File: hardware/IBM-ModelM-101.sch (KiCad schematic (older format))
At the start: 22 parts

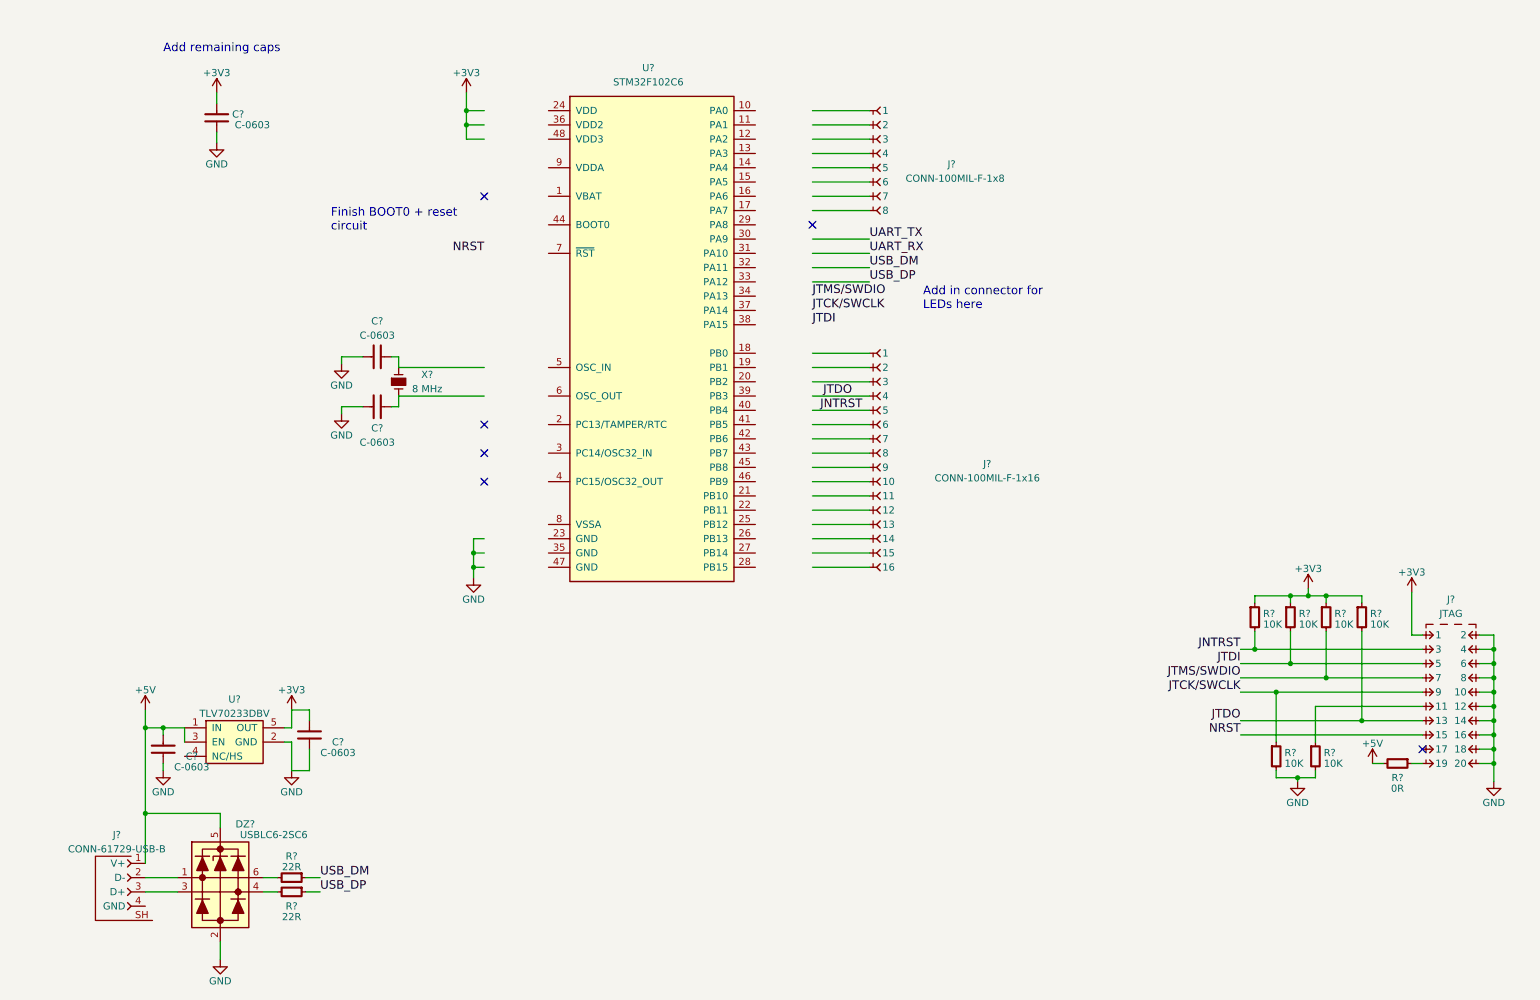
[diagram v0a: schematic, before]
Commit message: Finished power and boot/reset circuits
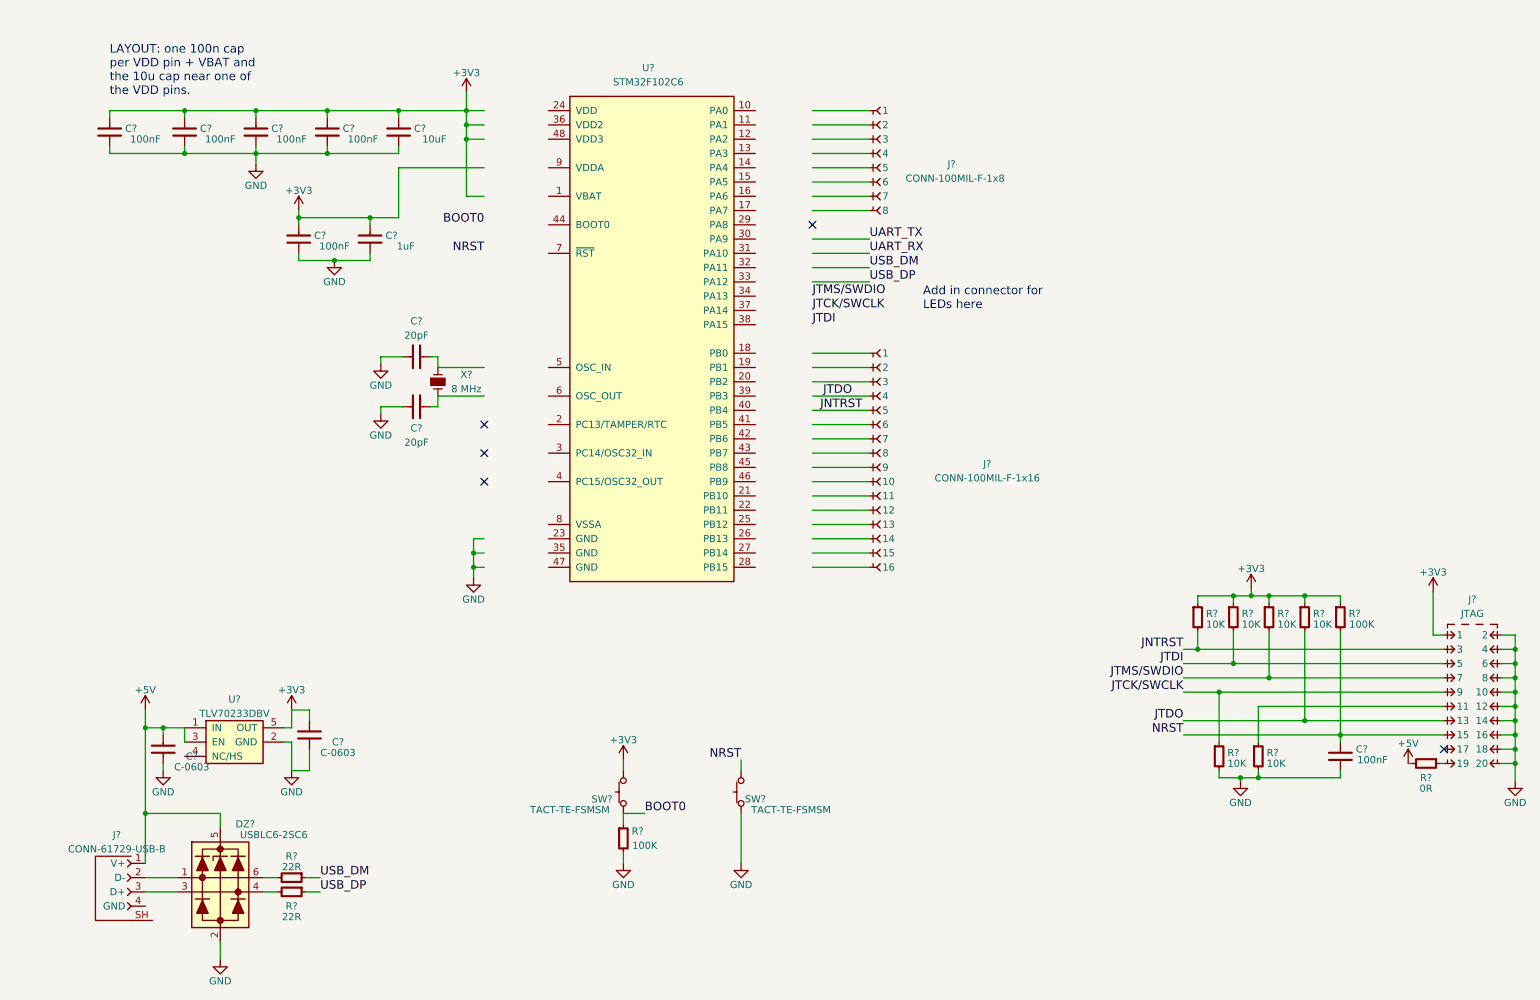
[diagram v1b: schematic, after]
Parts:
- added C? (x5): 100nF, IPC7351-Nominal:CAPC1608X55, symbol C-0603
- added C?: 10uF, IPC7351-Nominal:CAPC1608X55, symbol C-0603
- added C?: 1uF, IPC7351-Nominal:CAPC1608X55, symbol C-0603
- added R? (x2): 100K, IPC7351-Nominal:RESC1608X50, symbol R-0603
- added SW? (x2): TACT-TE-FSMSM, manuf:TE-FSMSM, symbol TACT-TE-FSMSM
- C? (x2): value C-0603 -> 20pF
- C?: value C-0603 -> 100nF
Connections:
- net labels added: BOOT0
- wire segments 108 -> 177
- no-connect marks 6 -> 5
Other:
- note added: "LAYOUT: one 100n cap\nper VDD pin + VBAT and\nthe 10u cap near one of \nthe VDD pins."
- note removed: "Add remaining caps"
- note removed: "Finish BOOT0 + reset\ncircuit"
- moved on the sheet: C?, J?, R?, X?

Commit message: Finished schematic, started work on PCB layout
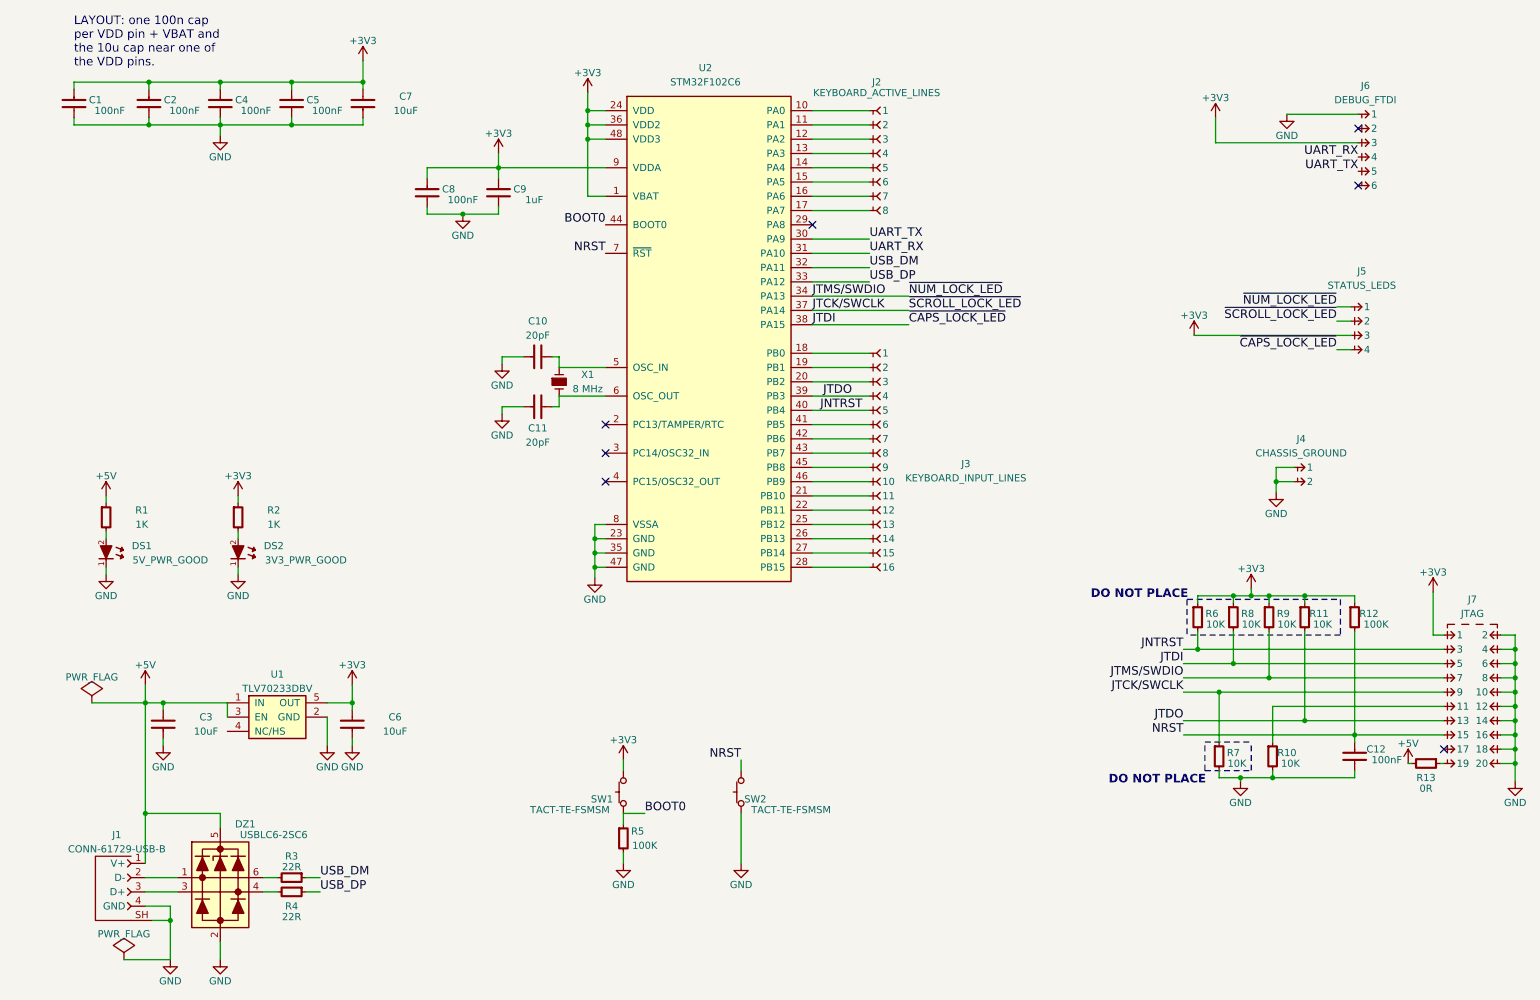
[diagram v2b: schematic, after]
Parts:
- removed C? (x2): C-0603, IPC7351-Nominal:CAPC1608X55, symbol C-0603
- removed C?: 10uF, IPC7351-Nominal:CAPC1608X55, symbol C-0603
- added C3, C6, C7: 10uF, IPC7351-Nominal:CAPC2012X70, symbol C-0805
- added DS1: 5V_PWR_GOOD, smd-semi:LED-0603, symbol LED-0603
- added DS2: 3V3_PWR_GOOD, smd-semi:LED-0603, symbol LED-0603
- added J4: CHASSIS_GROUND, conn-100mil:CONN-100MIL-M-1x2, symbol CONN-100MIL-M-1x2
- added J5: STATUS_LEDS, conn-100mil:CONN-100MIL-M-1x4-SHROUD, symbol CONN-100MIL-M-1x4-SHROUD
- added J6: DEBUG_FTDI, conn-100mil:CONN-100MIL-M-1x6, symbol CONN-100MIL-M-1x6
- added R1, R2: 1K, IPC7351-Nominal:RESC1608X50, symbol R-0603
- C1, C12, C2, C4, C5, C8: renamed from C?; BOM CAP MLCC 100pF C0G 50V 5% [0603] -> CAP MLCC 100nF C0G 6.3V 5% [0603]
- C9: renamed from C?; BOM CAP MLCC 100pF C0G 50V 5% [0603] -> CL10B105KQ8NNNC
- J2: renamed from J?; value CONN-100MIL-F-1x8 -> KEYBOARD_ACTIVE_LINES
- J3: renamed from J?; value CONN-100MIL-F-1x16 -> KEYBOARD_INPUT_LINES
- X1: renamed from X?; BOM (none) -> ATS08ASM-1E
- gave numbers to parts that had none: 20
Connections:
- net labels added: ~CAPS_LOCK_LED~, ~NUM_LOCK_LED~, ~SCROLL_LOCK_LED~
- wire segments 177 -> 155
- no-connect marks 5 -> 7
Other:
- note added: "DO NOT PLACE"
- note removed: "Add in connector for\nLEDs here"
- moved on the sheet: C1, C10, C11, C12, C2, C4, C5, C8, C9, R10, R12, U1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

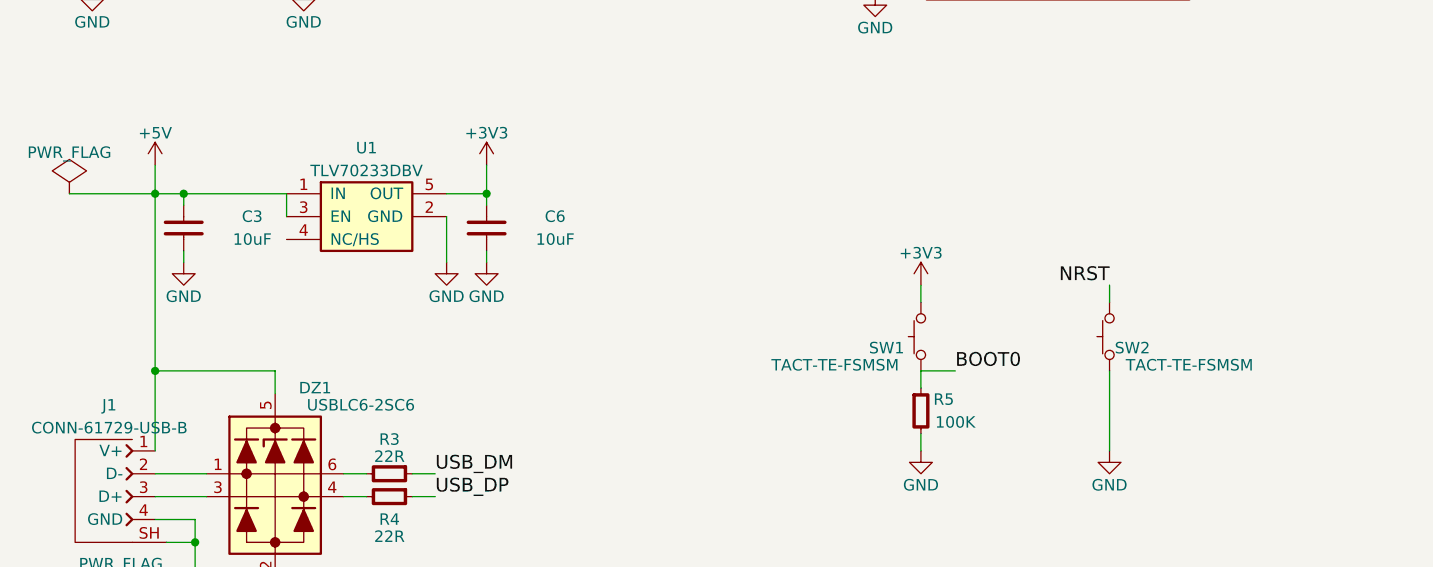
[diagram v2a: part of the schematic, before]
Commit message: Working on PCB layout
Placement is done. Most of the power, decoupling and support routing
finished.
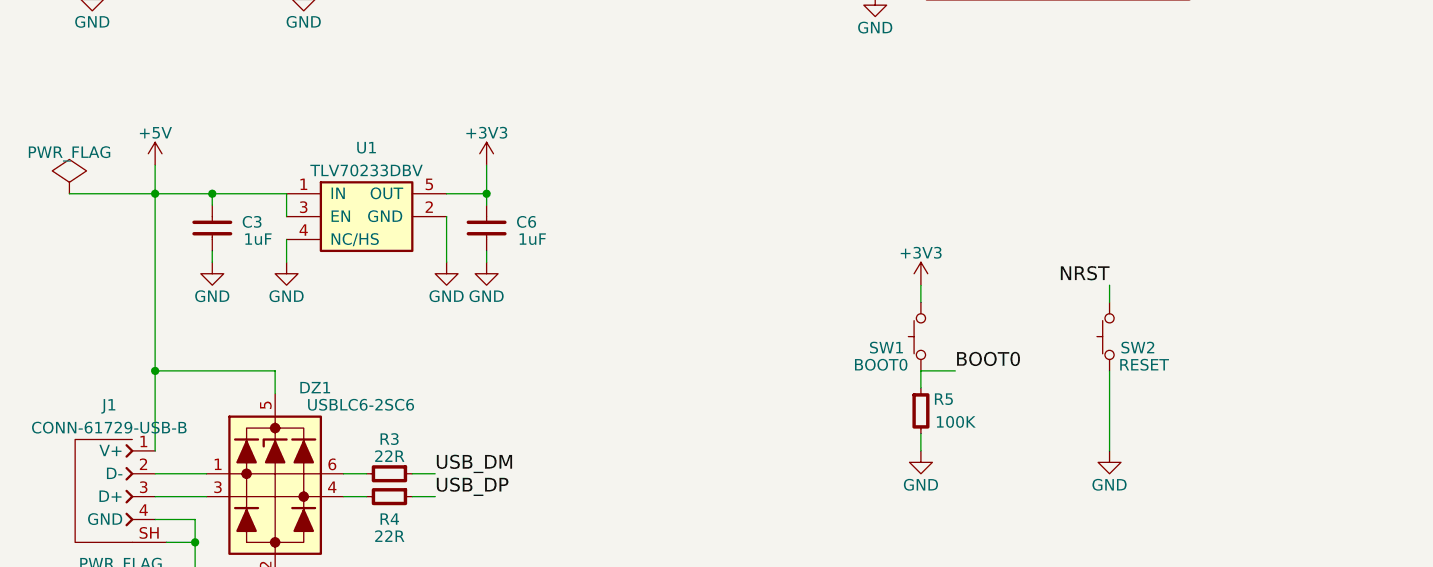
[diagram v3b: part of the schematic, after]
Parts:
- C3, C6: value 10uF -> 1uF; BOM GRM21BR61A106ME19L -> GRM219R61A105KA01D
- SW1: value TACT-TE-FSMSM -> BOOT0
- SW2: value TACT-TE-FSMSM -> RESET
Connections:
- net GND: now also U1.4 (NC/HS)
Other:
- moved on the sheet: C3

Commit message: Re-working crystal selection and routing.
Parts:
- removed X1: 8 MHz, IPC7351-Nominal:XTAL1200X480X460, symbol XTAL-HC49US-SMD
- added X1: 8MHz, IPC7351-Nominal:RESM9940X449, symbol XTAL-ABRACON-ABM2
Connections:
- net at C10.1, U2.5 (OSC_IN): now also X1.1
- net at C11.1, U2.6 (OSC_OUT): now also X1.2
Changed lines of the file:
@@
-$EndComp
-$Comp
-L XTAL-HC49US-SMD X1
-U 1 1 573D2351
-P 4325 3400
-F 0 "X1" H 4525 3450 50  0000 C CNN
-F 1 "8 MHz" H 4525 3350 50  0000 C CNN
-F 2 "IPC7351-Nominal:XTAL1200X480X460" H 4425 3350 60  0001 C CNN
-F 3 "" H 4325 3400 60  0000 C CNN
-F 4 "ATS08ASM-1E" H 4325 3400 60  0001 C CNN "BOM"
-	1    4325 3400
-	1    0    0    -1
 $EndComp
 $Comp
@@
 Wire Wire Line
 	2000 5850 2000 5950
+$Comp
+L XTAL-ABRACON-ABM2 X1
+U 1 1 5745E041
+P 4325 3400
+F 0 "X1" H 4525 3450 50  0000 C CNN
+F 1 "8MHz" H 4525 3350 50  0000 C CNN
+F 2 "IPC7351-Nominal:RESM9940X449" H 4425 3350 60  0001 C CNN
+F 3 "" H 4325 3400 60  0000 C CNN
+F 4 "ABM2-8.000MHZ-D4Y-T" H 4325 3400 60  0001 C CNN "BOM"
+	1    4325 3400
+	1    0    0    -1
+$EndComp
 $EndSCHEMATC

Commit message: Finished PCB layout
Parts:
- J1: value CONN-61729-USB-B -> CONN-MOLEX-0670688000-USB-B; footprint conn-fci:CONN-61729 -> conn-molex:CONN-MOLEX-0670688000-USB_B
- X1: footprint IPC7351-Nominal:RESM9940X449 -> smd-non-ipc:Abracon-ABM2
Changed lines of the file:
@@
 P 1225 6975
 F 0 "J1" H 1225 7375 50  0000 C CNN
-F 1 "CONN-61729-USB-B" H 1225 7275 50  0000 C CNN
-F 2 "conn-fci:CONN-61729" H 1225 7475 50  0001 C CNN
+F 1 "CONN-MOLEX-0670688000-USB-B" H 1225 7275 50  0000 C CNN
+F 2 "conn-molex:CONN-MOLEX-0670688000-USB_B" H 1225 7475 50  0001 C CNN
 F 3 "" H 1125 7175 50  0000 C CNN
 F 4 "DIST DIGIKEY 609-3657-ND" H 1225 7575 50  0001 C CNN "BOM"
@@
 $Comp
 L XTAL-ABRACON-ABM2 X1
-U 1 1 5745E041
+U 1 1 5750E5AF
 P 4325 3400
 F 0 "X1" H 4525 3450 50  0000 C CNN
 F 1 "8MHz" H 4525 3350 50  0000 C CNN
-F 2 "IPC7351-Nominal:RESM9940X449" H 4425 3350 60  0001 C CNN
+F 2 "smd-non-ipc:Abracon-ABM2" H 4425 3350 60  0001 C CNN
 F 3 "" H 4325 3400 60  0000 C CNN
 F 4 "ABM2-8.000MHZ-D4Y-T" H 4325 3400 60  0001 C CNN "BOM"

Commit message: Updates + replaced tab header with correct footprint
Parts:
- J4: footprint conn-100mil:CONN-100MIL-M-1x2 -> conn-molex:CONN-MOLEX-0197134001-TAB
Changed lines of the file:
@@
 F 0 "J4" H 9525 4200 50  0000 C CNN
 F 1 "CHASSIS_GROUND" H 9525 4100 50  0000 C CNN
-F 2 "conn-100mil:CONN-100MIL-M-1x2" H 9525 4000 50  0001 C CNN
+F 2 "conn-molex:CONN-MOLEX-0197134001-TAB" H 9525 4000 50  0001 C CNN
 F 3 "" H 9525 4000 50  0000 C CNN
 	1    9525 4000

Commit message: Final fixes to schematic and PCB layout
Fixed silk screen errors, added pin-out information to I/O headers and
JTAG.
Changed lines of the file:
@@
 F 0 "U2" H 5350 5000 50  0000 C CNN
 F 1 "STM32F102C6" H 5350 4900 50  0000 C CNN
-F 2 "IPC7351-Nominal:QFP50P900X900X160-48" H 5350 5050 50  0001 C CNN
+F 2 "IPC7351-Nominal:QFP50P900X900X160-48" H 5375 5125 50  0000 C CNN
 F 3 "" H 5350 5050 50  0000 C CNN
-F 4 "IC ST STM32F102C6" H 5850 5450 50  0001 C CNN "BOM"
+F 4 "IC ST STM32F102C6" H 5375 5225 50  0000 C CNN "BOM"
 	1    5350 3100
 	1    0    0    -1
@@
 F 0 "U1" H 2350 5950 50  0000 C CNN
 F 1 "TLV70233DBV" H 2350 5850 50  0000 C CNN
-F 2 "smd-semi:SOT-23-5" H 2350 5500 50  0001 C CNN
+F 2 "smd-semi:SOT-23-5" H 2350 6050 50  0000 C CNN
 F 3 "" H 2350 5700 60  0000 C CNN
-F 4 "IC TI TLV702vvDBV" H 2350 5400 60  0001 C CNN "BOM"
+F 4 "IC TI TLV702vvDBV" H 2350 6150 60  0000 C CNN "BOM"
 	1    2350 5700
 	1    0    0    -1

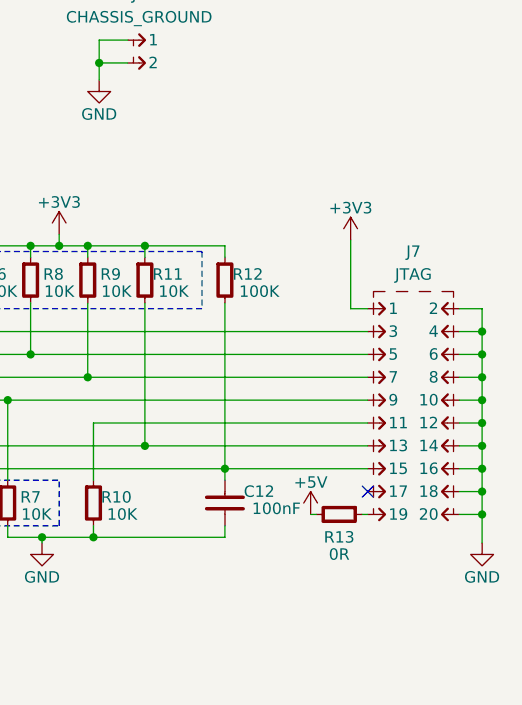
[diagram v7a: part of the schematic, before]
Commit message: Converting to STM32F102
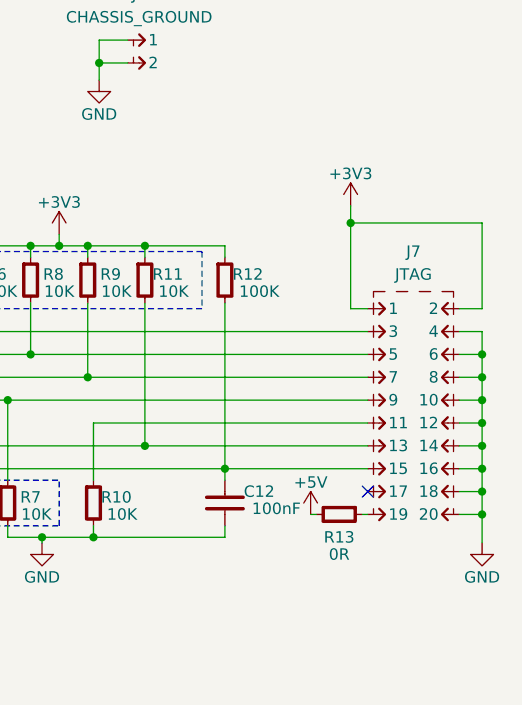
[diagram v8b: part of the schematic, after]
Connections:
- net +3V3: now also J7.2
- net GND: no longer J7.2
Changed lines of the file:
@@
 L +3V3 #PWR010
 U 1 1 573DDDD0
-P 10450 4875
-F 0 "#PWR010" H 10450 4725 50  0001 C CNN
-F 1 "+3V3" H 10450 5015 50  0000 C CNN
-F 2 "" H 10450 4875 50  0000 C CNN
-F 3 "" H 10450 4875 50  0000 C CNN
-	1    10450 4875
+P 10450 4725
+F 0 "#PWR010" H 10450 4575 50  0001 C CNN
+F 1 "+3V3" H 10450 4865 50  0000 C CNN
+F 2 "" H 10450 4725 50  0000 C CNN
+F 3 "" H 10450 4725 50  0000 C CNN
+	1    10450 4725
 	1    0    0    -1
 $EndComp
@@
 	1    0    0    -1
 $EndComp
+$Comp
+L GND #PWR034
+U 1 1 5743B0ED
+P 2000 5950
+F 0 "#PWR034" H 2000 5700 50  0001 C CNN
+F 1 "GND" H 2000 5800 50  0000 C CNN
+F 2 "" H 2000 5950 50  0000 C CNN
+F 3 "" H 2000 5950 50  0000 C CNN
+	1    2000 5950
+	1    0    0    -1
+$EndComp
+$Comp
+L XTAL-ABRACON-ABM2 X1
+U 1 1 5750E5AF
+P 4325 3400
+F 0 "X1" H 4525 3450 50  0000 C CNN
+F 1 "8MHz" H 4525 3350 50  0000 C CNN
+F 2 "smd-non-ipc:Abracon-ABM2" H 4425 3350 60  0001 C CNN
+F 3 "" H 4325 3400 60  0000 C CNN
+F 4 "ABM2-8.000MHZ-D4Y-T" H 4325 3400 60  0001 C CNN "BOM"
+	1    4325 3400
+	1    0    0    -1
+$EndComp
 Wire Wire Line
 	4275 3575 4325 3575
@@
 	11025 6075 10925 6075
 Wire Wire Line
-	11025 5175 11025 6200
-Wire Wire Line
 	10925 5975 11025 5975
 Connection ~ 11025 6075
@@
 Connection ~ 11025 5375
 Wire Wire Line
-	10925 5175 11025 5175
-Connection ~ 11025 5275
-Wire Wire Line
 	10525 5175 10450 5175
 Wire Wire Line
-	10450 5175 10450 4875
+	10450 5175 10450 4725
 Wire Wire Line
 	8700 5275 10525 5275
@@
 Wire Wire Line
 	2075 4700 2075 4750
-$Comp
-L GND #PWR034
-U 1 1 5743B0ED
-P 2000 5950
-F 0 "#PWR034" H 2000 5700 50  0001 C CNN
-F 1 "GND" H 2000 5800 50  0000 C CNN
-F 2 "" H 2000 5950 50  0000 C CNN
-F 3 "" H 2000 5950 50  0000 C CNN
-	1    2000 5950
-	1    0    0    -1
-$EndComp
 Wire Wire Line
 	2000 5850 2000 5950
-$Comp
-L XTAL-ABRACON-ABM2 X1
-U 1 1 5750E5AF
-P 4325 3400
-F 0 "X1" H 4525 3450 50  0000 C CNN
-F 1 "8MHz" H 4525 3350 50  0000 C CNN
-F 2 "smd-non-ipc:Abracon-ABM2" H 4425 3350 60  0001 C CNN
-F 3 "" H 4325 3400 60  0000 C CNN
-F 4 "ABM2-8.000MHZ-D4Y-T" H 4325 3400 60  0001 C CNN "BOM"
-	1    4325 3400
-	1    0    0    -1
-$EndComp
+Wire Wire Line
+	10925 5175 11025 5175
+Wire Wire Line
+	11025 5175 11025 4800
+Wire Wire Line
+	11025 4800 10450 4800
+Connection ~ 10450 4800
+Wire Wire Line
+	11025 5275 11025 6200
 $EndSCHEMATC
